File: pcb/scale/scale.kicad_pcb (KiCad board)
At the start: 2 copper layers, 103.8 x 47.9 mm, 89 parts, among them J1 USB_C_Receptacle_USB2.0, J2 Conn_01x07, J3 Conn_01x04, SW1 SW_Push, SW10 SW_Push, SW11 SW_Push, SW12 SW_Push, SW13 SW_Push, SW14 SW_Push, SW15 SW_Push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

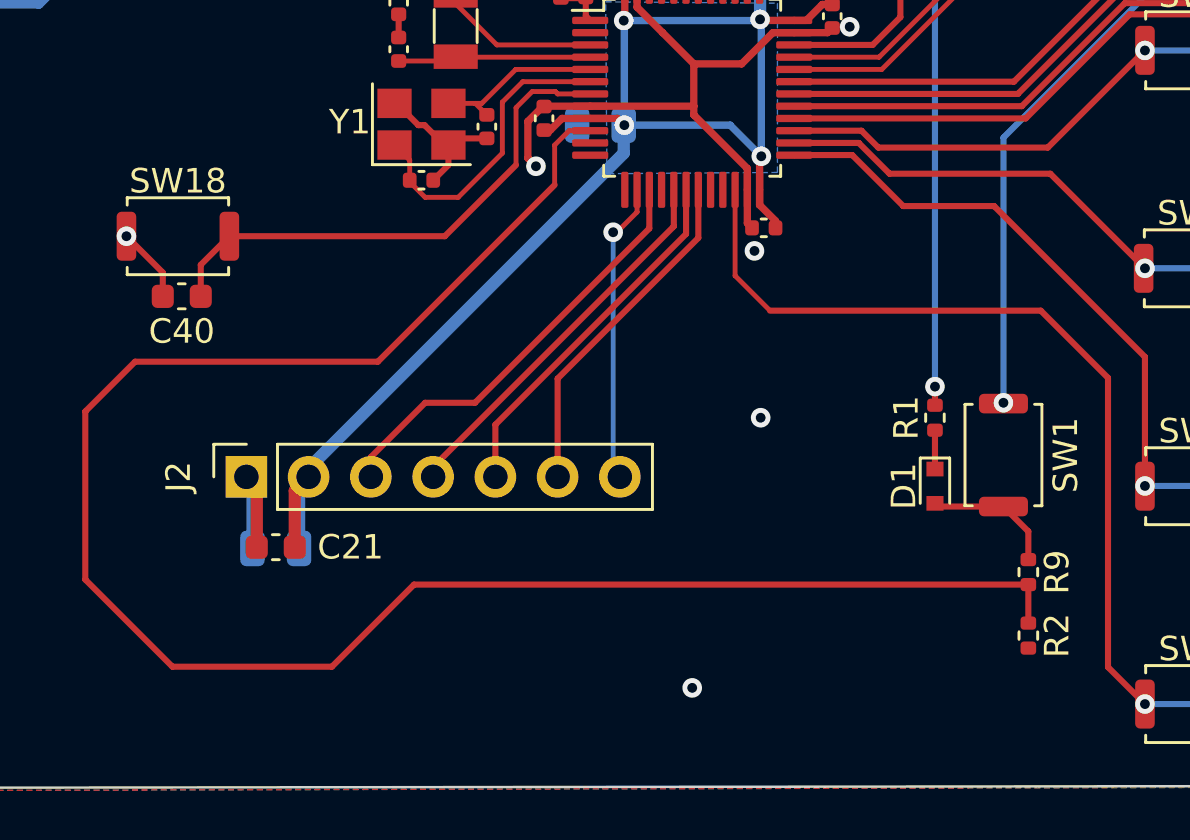
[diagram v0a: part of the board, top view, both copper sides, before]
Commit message: OLED屏排母向下移
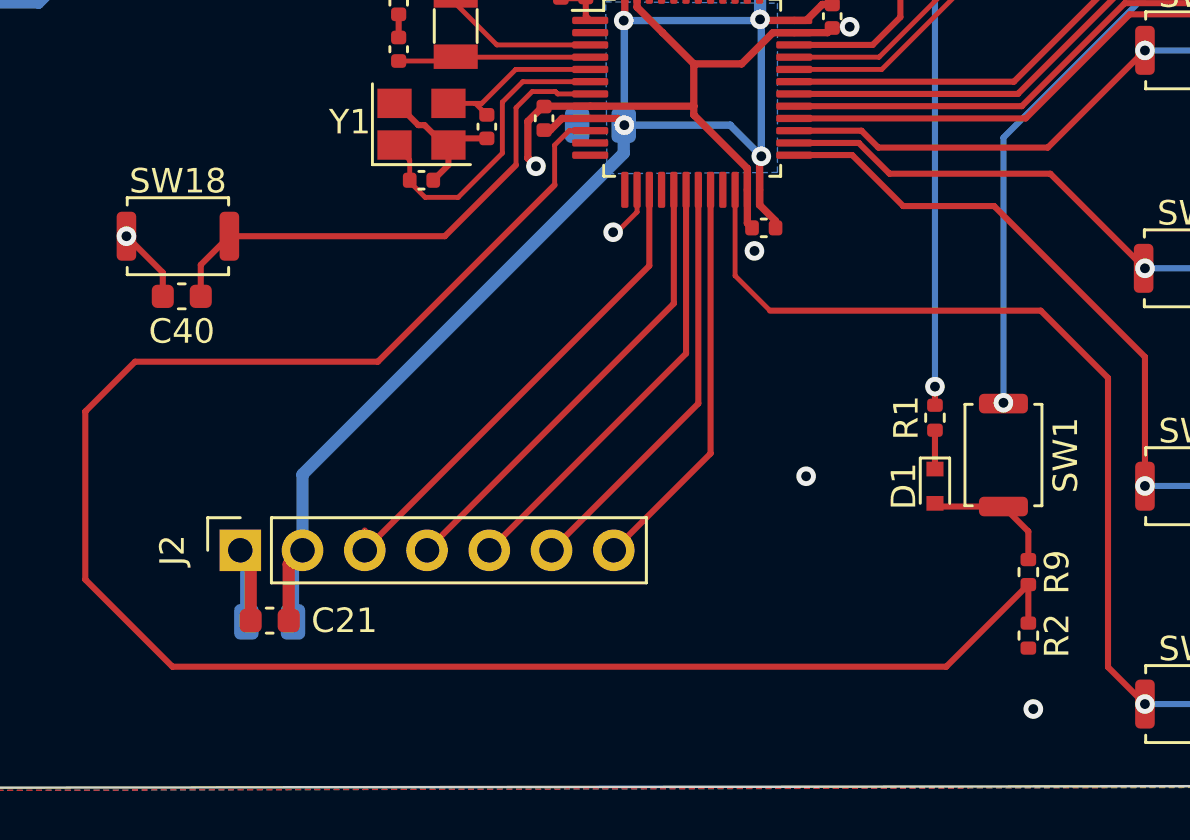
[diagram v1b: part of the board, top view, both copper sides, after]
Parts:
- moved C21 3.01 mm to (94.4, 91.8)
- moved J2 3.01 mm to (93.2, 89.0)
- moved C22 3.01 mm to (94.4, 91.9)
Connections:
- J2 pad 7: /NSS -> /CS_OLED
- U3 pad 20: unconnected-(U3-Pad20) -> /CS_OLED
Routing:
- net /CS_OLED: track 0.00 -> 16.7 mm
- net /NSS: track 12.3 -> 2.22 mm
- net /MOSI: track 15.8 -> 19.3 mm
- net +3V3: track 99.9 -> 103.4 mm
- net /RES: track 14.9 -> 18.0 mm
- net /DC: track 14.1 -> 17.2 mm
- net /SCK: track 17.6 -> 20.3 mm

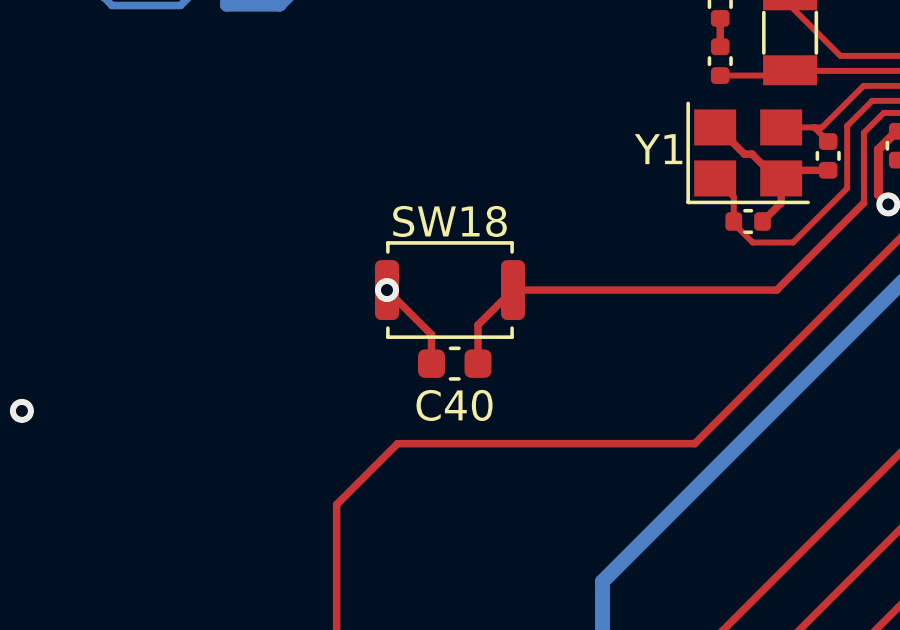
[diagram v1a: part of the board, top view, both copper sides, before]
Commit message: 翻转NRST按键
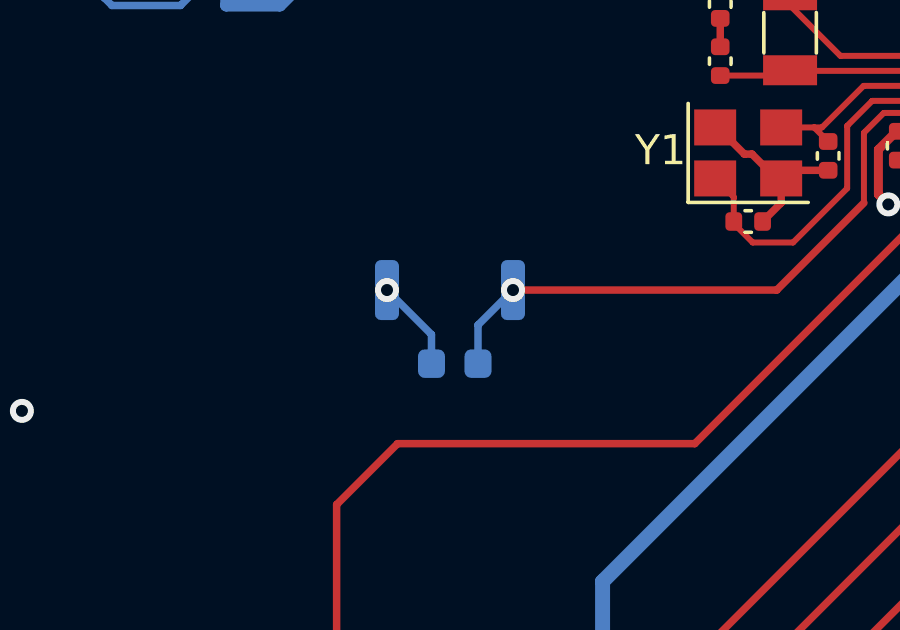
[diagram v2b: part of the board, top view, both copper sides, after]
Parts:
- C40, SW18: moved to B.Cu
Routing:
- net /NRST: vias 0 -> 1

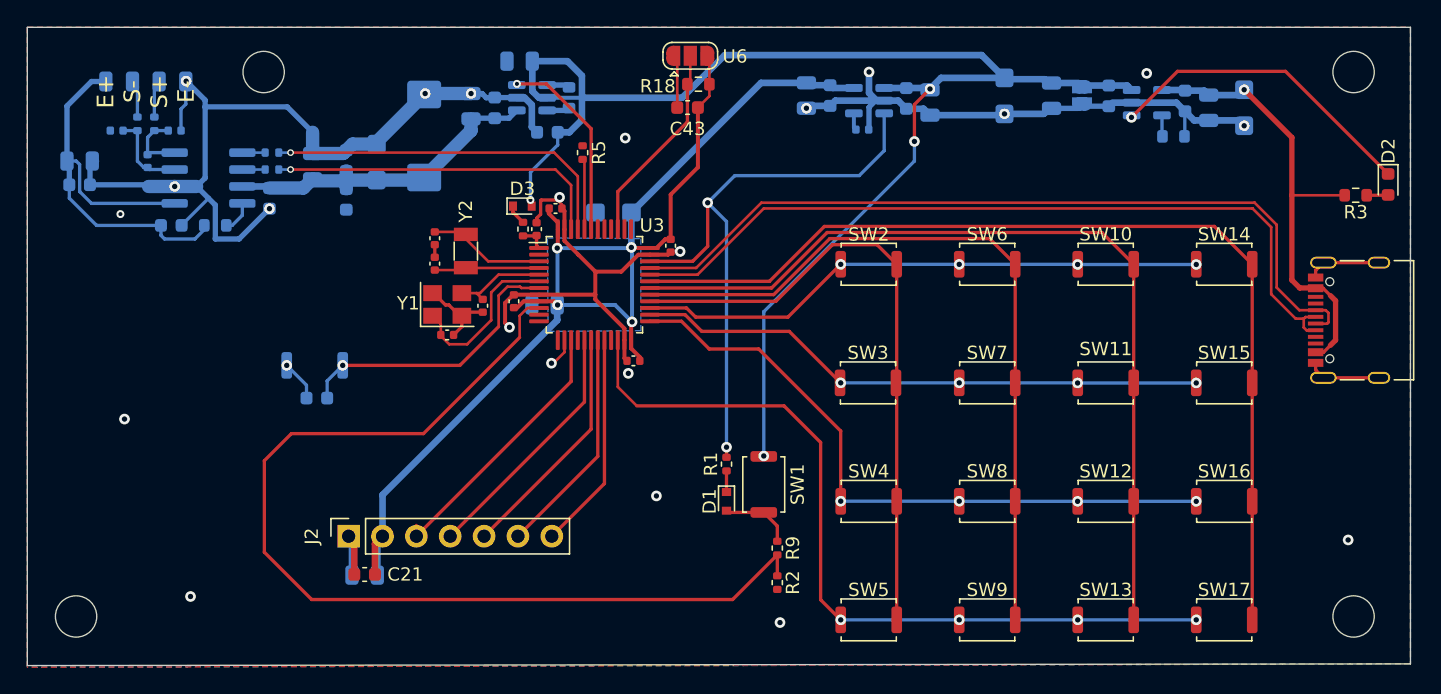
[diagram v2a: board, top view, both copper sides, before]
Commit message: 修复一些DRC错误和警告
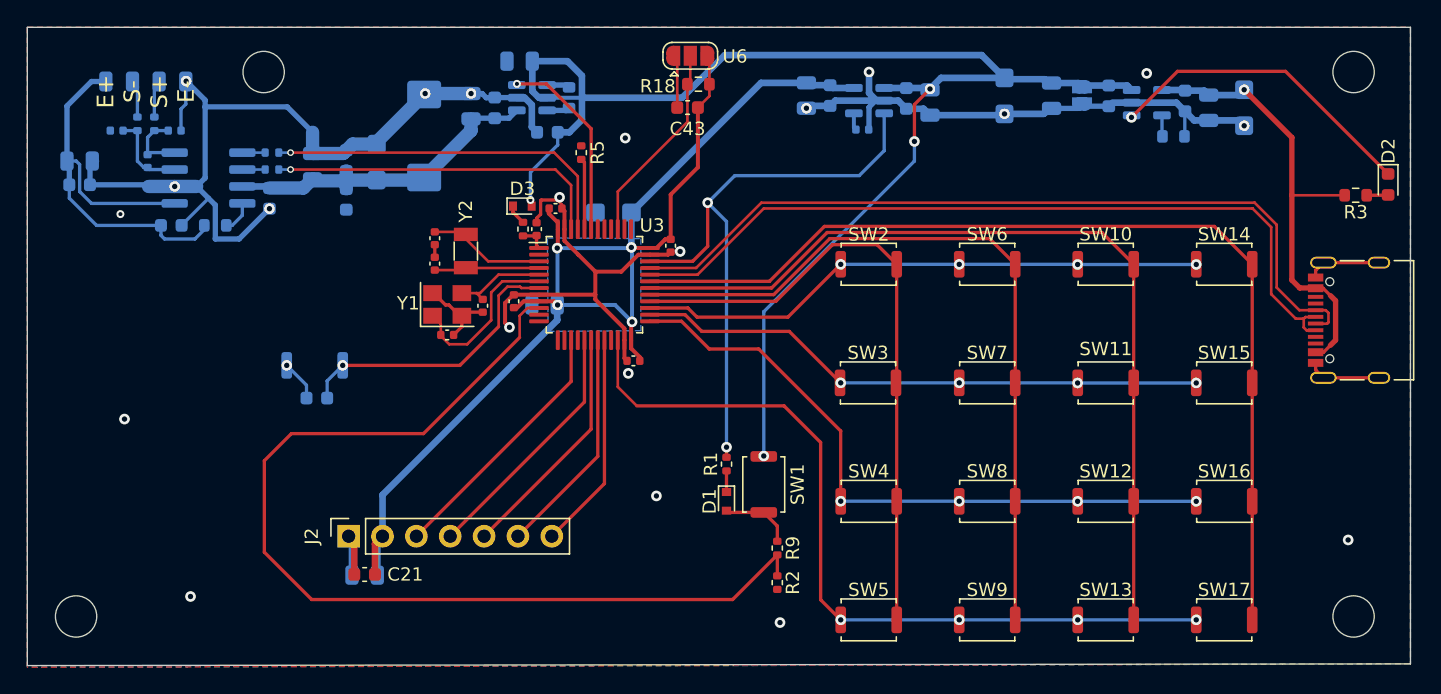
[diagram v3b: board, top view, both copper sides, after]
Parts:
- moved R5 0.10 mm to (110.6, 60.2)
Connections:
- U3 pad 14: /NSS -> unconnected-(U3-Pad14)
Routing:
- net /NSS: track 2.22 -> 0.00 mm, vias 1 -> 0
- net /SCK: track 20.3 -> 19.5 mm
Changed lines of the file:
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@@
   (net 57 "/RES")
   (net 58 "/DC")
-  (net 59 "/NSS")
+  (net 59 "unconnected-(U3-Pad14)")
   (net 60 "/Line_18B20")
   (net 61 "unconnected-(U3-Pad2)")
@@
   )
   (footprint "Resistor_SMD:R_0402_1005Metric" (layer "F.Cu")
-    (at 110.744 60.198 90)
+    (at 110.6424 60.198 90)
     (descr "Resistor SMD 0402 (1005 Metric), square (rectangular) end terminal, IPC_7351 nominal, (Body size source: IPC-SM-782 page 72, https://www.pcb-3d.com/wordpress/wp-content/uploads/ipc-sm-782a_amendment_1_and_2.pdf), generated with kicad-footprint-generator")
     (tags "resistor")
@@
       (net 66 "unconnected-(U3-Pad13)") (pinfunction "PA3") (pintype "bidirectional"))
     (pad "14" smd roundrect (at -2.25 4.1625) (size 0.3 1.475) (layers "F.Cu" "F.Paste" "F.Mask") (roundrect_rratio 0.25)
-      (net 59 "/NSS") (pinfunction "PA4") (pintype "bidirectional"))
+      (net 59 "unconnected-(U3-Pad14)") (pinfunction "PA4") (pintype "bidirectional"))
     (pad "15" smd roundrect (at -1.75 4.1625) (size 0.3 1.475) (layers "F.Cu" "F.Paste" "F.Mask") (roundrect_rratio 0.25)
       (net 36 "/SCK") (pinfunction "PA5") (pintype "bidirectional"))
@@
   (segment (start 148.3724 56.7188) (end 148.209 56.5554) (width 0.4) (layer "B.Cu") (net 2))
   (segment (start 80.6605 65.646) (end 82.6795 63.627) (width 0.25) (layer "B.Cu") (net 2))
-  (segment (start 81.002 54.8372) (end 80.978 54.8132) (width 0.4) (layer "B.Cu") (net 2))
   (segment (start 135.0264 56.909) (end 136.3246 56.909) (width 0.5) (layer "B.Cu") (net 2))
   (segment (start 132.2324 56.7944) (end 132.2324 58.4428) (width 0.4) (layer "B.Cu") (net 2))
@@
   (segment (start 114.383 74.886) (end 115.034 75.537) (width 0.3) (layer "F.Cu") (net 5))
   (segment (start 114.383 72.9674) (end 114.4524 72.898) (width 0.3) (layer "F.Cu") (net 5))
-  (segment (start 114.3948 67.354) (end 114.3508 67.31) (width 0.3) (layer "F.Cu") (net 5))
   (segment (start 115.7955 67.354) (end 116.29 67.354) (width 0.3) (layer "F.Cu") (net 5))
   (segment (start 117.348 66.703) (end 117.348 63.3476) (width 0.3) (layer "F.Cu") (net 5))
@@
   (via (at 108.8644 71.628) (size 0.8) (drill 0.4) (layers "F.Cu" "B.Cu") (free) (net 5))
   (via (at 114.4016 67.31) (size 0.8) (drill 0.4) (layers "F.Cu" "B.Cu") (free) (net 5))
-  (segment (start 95.7326 88.6256) (end 95.7326 88.9762) (width 0.5) (layer "B.Cu") (net 5))
   (segment (start 108.8644 71.628) (end 113.1824 71.628) (width 0.3) (layer "B.Cu") (net 5))
-  (segment (start 95.7326 88.9762) (end 95.7326 85.8774) (width 0.5) (layer "B.Cu") (net 5))
   (segment (start 127.5334 54.9678) (end 124.1314 54.9678) (width 0.5) (layer "B.Cu") (net 5))
   (segment (start 127.7084 55.1428) (end 127.5334 54.9678) (width 0.5) (layer "B.Cu") (net 5))
@@
   (segment (start 114.4016 64.6976) (end 114.4054 64.6938) (width 0.5) (layer "B.Cu") (net 5))
   (segment (start 108.839 71.628) (end 108.839 72.771) (width 0.5) (layer "B.Cu") (net 5))
+  (segment (start 95.7326 85.8774) (end 95.7326 88.9762) (width 0.5) (layer "B.Cu") (net 5))
   (segment (start 95.3418 89.367) (end 95.7326 88.9762) (width 0.5) (layer "B.Cu") (net 5))
   (segment (start 129.3114 55.1428) (end 127.7084 55.1428) (width 0.5) (layer "B.Cu") (net 5))
@@
   (segment (start 154.2059 57.4018) (end 154.2059 58.9303) (width 0.25) (layer "B.Cu") (net 15))
   (segment (start 121.539 85.66) (end 121.539 84.076) (width 0.25) (layer "F.Cu") (net 16))
-  (segment (start 110.883 60.847) (end 110.744 60.708) (width 0.2) (layer "F.Cu") (net 17))
-  (segment (start 110.883 65.9415) (end 110.883 60.847) (width 0.2) (layer "F.Cu") (net 17))
+  (segment (start 110.883 65.9415) (end 110.883 60.9486) (width 0.25) (layer "F.Cu") (net 17))
+  (segment (start 110.883 60.9486) (end 110.6424 60.708) (width 0.25) (layer "F.Cu") (net 17))
   (segment (start 105.5228 64.6756) (end 106.2736 65.4264) (width 0.25) (layer "F.Cu") (net 18))
   (segment (start 105.5228 64.2112) (end 105.5228 64.6756) (width 0.25) (layer "F.Cu") (net 18))
@@
   (segment (start 112.383 85.0258) (end 108.4326 88.9762) (width 0.25) (layer "F.Cu") (net 22))
   (segment (start 112.383 74.2665) (end 112.383 85.0258) (width 0.25) (layer "F.Cu") (net 22))
-  (segment (start 108.1586 88.7022) (end 108.4326 88.9762) (width 0.2) (layer "B.Cu") (net 22))
   (segment (start 106.0196 72.4408) (end 106.0196 74.0664) (width 0.2) (layer "F.Cu") (net 24))
   (segment (start 106.0196 74.0664) (end 98.806 81.28) (width 0.25) (layer "F.Cu") (net 24))
@@
   (segment (start 106.6064 71.854) (end 106.0196 72.4408) (width 0.2) (layer "F.Cu") (net 24))
   (segment (start 107.4705 71.854) (end 106.6064 71.854) (width 0.2) (layer "F.Cu") (net 24))
-  (segment (start 115.7955 71.854) (end 118.5392 71.854) (width 0.25) (layer "F.Cu") (net 26))
-  (segment (start 126.1446 72.5424) (end 130.107 68.58) (width 0.25) (layer "F.Cu") (net 26))
-  (segment (start 119.2276 72.5424) (end 126.1446 72.5424) (width 0.25) (layer "F.Cu") (net 26))
-  (segment (start 118.5392 71.854) (end 119.2276 72.5424) (width 0.25) (layer "F.Cu") (net 26))
+  (segment (start 118.6408 71.854) (end 115.7955 71.854) (width 0.25) (layer "F.Cu") (net 26))
+  (segment (start 126.1446 72.5424) (end 119.3292 72.5424) (width 0.25) (layer "F.Cu") (net 26))
+  (segment (start 130.107 68.58) (end 126.1446 72.5424) (width 0.25) (layer "F.Cu") (net 26))
+  (segment (start 119.3292 72.5424) (end 118.6408 71.854) (width 0.25) (layer "F.Cu") (net 26))
   (via (at 138.997 68.58) (size 0.8) (drill 0.4) (layers "F.Cu" "B.Cu") (net 26))
   (via (at 147.877 68.59) (size 0.8) (drill 0.4) (layers "F.Cu" "B.Cu") (net 26))
@@
   (segment (start 109.883 77.3658) (end 98.2726 88.9762) (width 0.25) (layer "F.Cu") (net 36))
   (segment (start 109.883 74.2665) (end 109.883 77.3658) (width 0.25) (layer "F.Cu") (net 36))
-  (segment (start 98.2726 88.1684) (end 98.2726 88.9762) (width 0.25) (layer "F.Cu") (net 36))
   (segment (start 110.883 78.9058) (end 100.8126 88.9762) (width 0.25) (layer "F.Cu") (net 37))
   (segment (start 110.883 74.2665) (end 110.883 78.9058) (width 0.25) (layer "F.Cu") (net 37))
-  (segment (start 100.8126 88.9762) (end 100.8126 88.5748) (width 0.25) (layer "F.Cu") (net 37))
   (segment (start 88.83775 60.198) (end 108.6104 60.198) (width 0.2) (layer "F.Cu") (net 38))
   (segment (start 110.383 61.9706) (end 110.383 65.9415) (width 0.2) (layer "F.Cu") (net 38))
@@
   (segment (start 111.883 74.2665) (end 111.883 82.9858) (width 0.25) (layer "F.Cu") (net 58))
   (segment (start 111.883 82.9858) (end 105.8926 88.9762) (width 0.25) (layer "F.Cu") (net 58))
-  (segment (start 108.5596 75.9968) (end 108.4072 75.9968) (width 0.2) (layer "F.Cu") (net 59))
-  (segment (start 109.383 74.2665) (end 109.383 75.1734) (width 0.2) (layer "F.Cu") (net 59))
-  (segment (start 109.383 75.1734) (end 108.5596 75.9968) (width 0.2) (layer "F.Cu") (net 59))
-  (via (at 108.4072 75.9968) (size 0.8) (drill 0.4) (layers "F.Cu" "B.Cu") (net 59))
-  (segment (start 118.6058 55.0672) (end 118.6058 57.8988) (width 0.25) (layer "F.Cu") (net 60))
-  (segment (start 113.383 63.1216) (end 113.383 65.9415) (width 0.25) (layer "F.Cu") (net 60))
+  (segment (start 118.6058 55.0672) (end 118.6058 57.8988) (width 0.2) (layer "F.Cu") (net 60))
+  (segment (start 113.383 63.1216) (end 113.383 65.9415) (width 0.2) (layer "F.Cu") (net 60))
   (segment (start 118.8212 52.9336) (end 118.8212 54.8518) (width 0.2) (layer "F.Cu") (net 60))
   (segment (start 118.8212 54.8518) (end 118.6058 55.0672) (width 0.2) (layer "F.Cu") (net 60))
-  (segment (start 118.6058 57.8988) (end 113.383 63.1216) (width 0.25) (layer "F.Cu") (net 60))
+  (segment (start 118.6058 57.8988) (end 113.383 63.1216) (width 0.2) (layer "F.Cu") (net 60))
   (zone (net 2) (net_name "GND") (layers F&B.Cu) (hatch edge 0.508)
     (connect_pads (clearance 0.254))
